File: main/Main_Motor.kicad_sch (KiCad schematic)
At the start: 3 parts

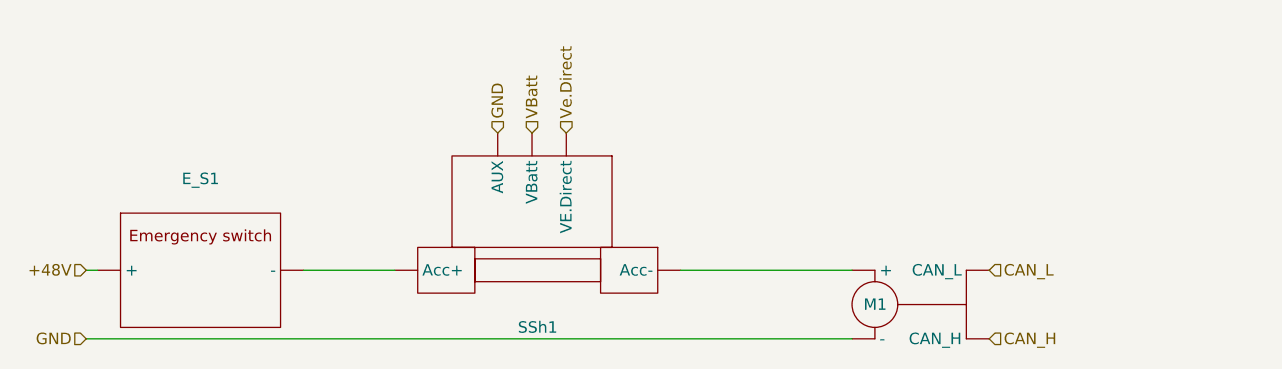
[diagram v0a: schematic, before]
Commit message: added UI, +12/gnd to 4 pin adapter symbol, added NMEA2000 gateway symbol
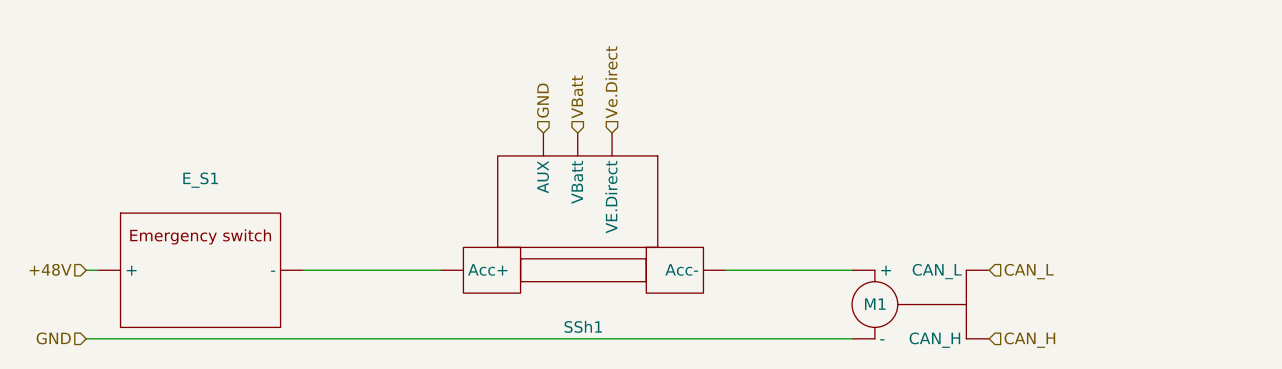
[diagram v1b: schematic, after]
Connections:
- new net: M1. (CAN_L), SSh1. (VE.Direct)
- new net: E_S1. (-), SSh1. (VE.Direct)
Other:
- moved on the sheet: SSh1
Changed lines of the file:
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@@
 	(wire
 		(pts
-			(xy 96.52 96.52) (xy 106.68 96.52)
+			(xy 143.51 96.52) (xy 157.48 96.52)
 		)
 		(stroke
@@
 	(wire
 		(pts
-			(xy 138.43 96.52) (xy 157.48 96.52)
+			(xy 111.76 96.52) (xy 96.52 96.52)
 		)
 		(stroke
@@
 	(hierarchical_label "GND"
 		(shape input)
-		(at 118.11 81.28 90)
+		(at 123.19 81.28 90)
 		(fields_autoplaced yes)
 		(effects
@@
 	(hierarchical_label "VBatt"
 		(shape input)
-		(at 121.92 81.28 90)
+		(at 127 81.28 90)
 		(fields_autoplaced yes)
 		(effects
@@
 	(hierarchical_label "Ve.Direct"
 		(shape input)
-		(at 125.73 81.28 90)
+		(at 130.81 81.28 90)
 		(fields_autoplaced yes)
 		(effects
@@
 	(symbol
 		(lib_id "New_Library_0:SmartShunt")
-		(at 121.92 88.9 270)
+		(at 127 88.9 270)
 		(unit 1)
 		(exclude_from_sim no)
@@
 		(fields_autoplaced yes)
 		(property "Reference" "SSh1"
-			(at 122.555 102.87 90)
+			(at 127.635 102.87 90)
 			(effects
 				(font
@@
 		)
 		(property "Value" "~"
-			(at 122.555 104.14 90)
+			(at 127.635 104.14 90)
 			(effects
 				(font
@@
 		)
 		(property "Footprint" ""
-			(at 122.555 95.885 90)
+			(at 127.635 95.885 90)
 			(effects
 				(font
@@
 		)
 		(property "Datasheet" ""
-			(at 122.555 95.885 90)
+			(at 127.635 95.885 90)
 			(effects
 				(font
@@
 		)
 		(property "Description" ""
-			(at 122.555 95.885 90)
+			(at 127.635 95.885 90)
 			(effects
 				(font

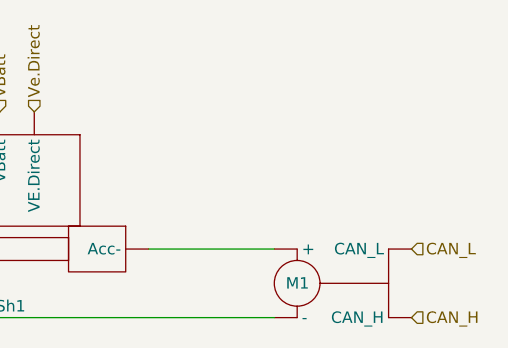
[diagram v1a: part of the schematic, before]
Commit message: added new output from main motor and connected it to NMEA input in monitor
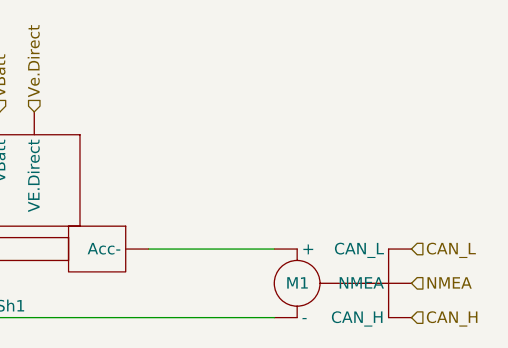
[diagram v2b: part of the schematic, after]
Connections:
- net NMEA: now reaches M1. (NMEA)
- net NMEA: no longer SSh1. (VE.Direct)
- new net: M1. (NMEA), SSh1. (VE.Direct)
- new net: E_S1. (-), SSh1. (VE.Direct)
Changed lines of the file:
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@@
+		)
+	)
+	(hierarchical_label "NMEA"
+		(shape input)
+		(at 172.72 100.33 0)
+		(fields_autoplaced yes)
+		(effects
+			(font
+				(size 1.27 1.27)
+			)
+			(justify left)
 		)
 	)
@@
 		)
 		(pin ""
+		)
+		(pin ""

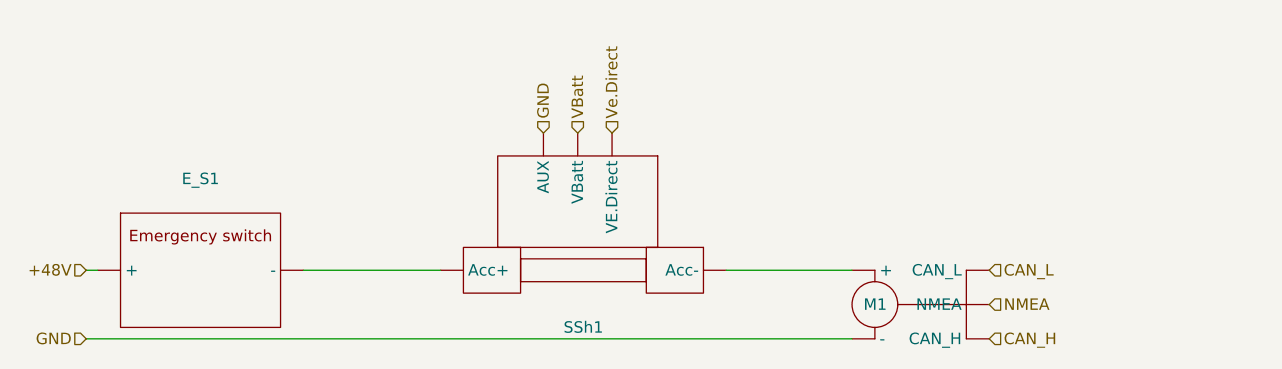
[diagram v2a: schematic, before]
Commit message: added emergency switch to mppt updateg seet layout
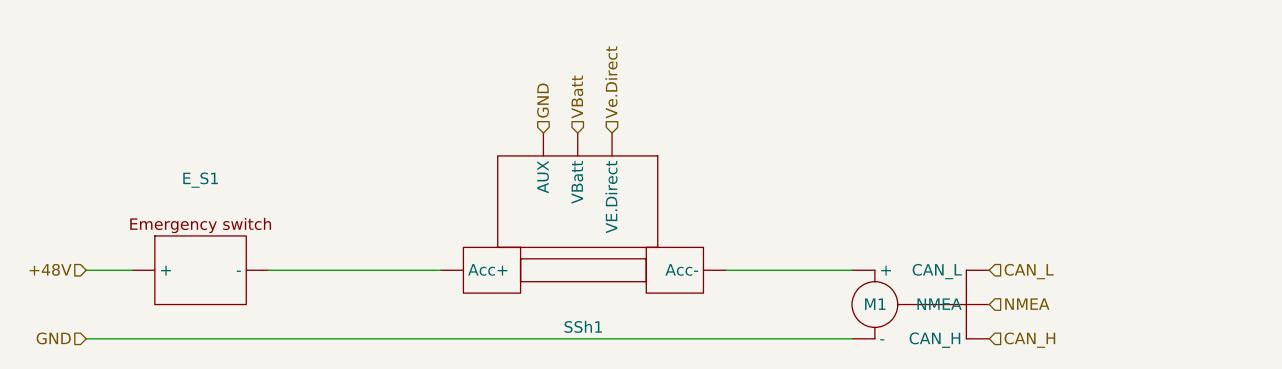
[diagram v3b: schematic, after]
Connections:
- new net: E_S1. (-), SSh1. (VE.Direct)
- new net: M1. (NMEA), SSh1. (VE.Direct)
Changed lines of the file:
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@@
 	(wire
 		(pts
-			(xy 73.66 96.52) (xy 72.39 96.52)
+			(xy 72.39 96.52) (xy 77.47 96.52)
 		)
 		(stroke
@@
 	(wire
 		(pts
-			(xy 72.39 104.14) (xy 157.48 104.14)
+			(xy 92.71 96.52) (xy 111.76 96.52)
 		)
 		(stroke
@@
 	(wire
 		(pts
-			(xy 143.51 96.52) (xy 157.48 96.52)
+			(xy 72.39 104.14) (xy 157.48 104.14)
 		)
 		(stroke
@@
 	(wire
 		(pts
-			(xy 111.76 96.52) (xy 96.52 96.52)
+			(xy 143.51 96.52) (xy 157.48 96.52)
 		)
 		(stroke
@@
 				(path "/54fbbba9-a737-4199-9a4b-f9fa49b3de5e/0e0ba13e-1f37-4579-8a2d-3eca3dc701e5"
 					(reference "SSh1")
+					(unit 1)
+				)
+			)
+		)
+	)
+	(symbol
+		(lib_id "New_Library_0:Emergency_Switch")
+		(at 85.09 96.52 0)
+		(unit 1)
+		(exclude_from_sim no)
+		(in_bom yes)
+		(on_board yes)
+		(dnp no)
+		(fields_autoplaced yes)
+		(property "Reference" "E_S1"
+			(at 85.09 86.36 0)
+			(effects
+				(font
+					(size 1.27 1.27)
+				)
+			)
+		)
+		(property "Value" "~"
+			(at 85.09 88.9 0)
+			(effects
+				(font
+					(size 1.27 1.27)
+				)
+			)
+		)
+		(property "Footprint" ""
+			(at 85.09 96.52 0)
+			(effects
+				(font
+					(size 1.27 1.27)
+				)
+				(hide yes)
+			)
+		)
+		(property "Datasheet" ""
+			(at 85.09 96.52 0)
+			(effects
+				(font
+					(size 1.27 1.27)
+				)
+				(hide yes)
+			)
+		)
+		(property "Description" ""
+			(at 85.09 96.52 0)
+			(effects
+				(font
+					(size 1.27 1.27)
+				)
+				(hide yes)
+			)
+		)
+		(pin ""
+		)
+		(pin ""
+		)
+		(instances
+			(project ""
+				(path "/54fbbba9-a737-4199-9a4b-f9fa49b3de5e/0e0ba13e-1f37-4579-8a2d-3eca3dc701e5"
+					(reference "E_S1")
 					(unit 1)
 				)
@@
 					(unit 1)
 				)
-			)
-		)
-	)
-	(symbol
-		(lib_id "New_Library_0:Emergency_Switch")
-		(at 85.09 96.52 0)
-		(unit 1)
-		(exclude_from_sim no)
-		(in_bom yes)
-		(on_board yes)
-		(dnp no)
-		(fields_autoplaced yes)
-		(property "Reference" "E_S1"
-			(at 85.09 86.36 0)
-			(effects
-				(font
-					(size 1.27 1.27)
-				)
-			)
-		)
-		(property "Value" "~"
-			(at 85.09 88.9 0)
-			(effects
-				(font
-					(size 1.27 1.27)
-				)
-			)
-		)
-		(property "Footprint" ""
-			(at 85.09 96.52 0)
-			(effects
-				(font
-					(size 1.27 1.27)
-				)
-				(hide yes)
-			)
-		)
-		(property "Datasheet" ""
-			(at 85.09 96.52 0)
-			(effects
-				(font
-					(size 1.27 1.27)
-				)
-				(hide yes)
-			)
-		)
-		(property "Description" ""
-			(at 85.09 96.52 0)
-			(effects
-				(font
-					(size 1.27 1.27)
-				)
-				(hide yes)
-			)
-		)
-		(pin ""
-		)
-		(pin ""
-		)
-		(instances
-			(project ""
-				(path "/54fbbba9-a737-4199-9a4b-f9fa49b3de5e/0e0ba13e-1f37-4579-8a2d-3eca3dc701e5"
-					(reference "E_S1")
-					(unit 1)
-				)

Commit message: added logos, oranised sheets, final version
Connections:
- new net: E_S1. (-), SSh1. (VE.Direct)
- new net: M1. (NMEA), SSh1. (VE.Direct)
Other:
- company: (none) -> Designers: Krzysztof Grajek, Wojtek Kołodziej
- title: (none) -> Main motor schematic

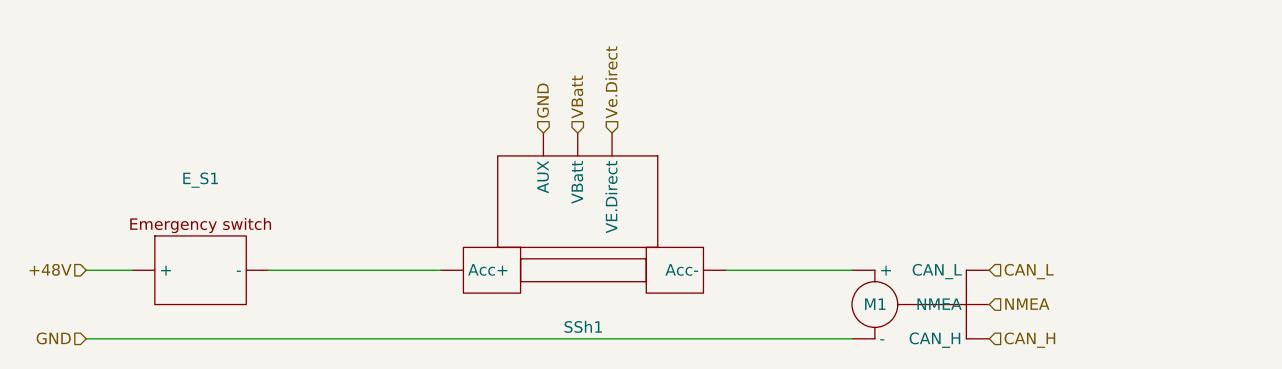
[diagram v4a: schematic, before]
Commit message: added nwe sheet (switching system), created a few new symbols, changed +48V coming from battery to Battery_High_voltage,
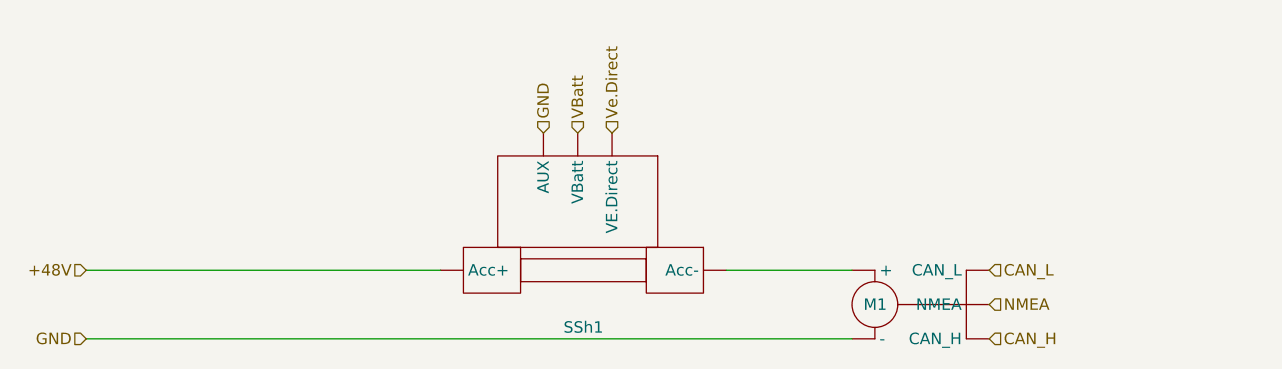
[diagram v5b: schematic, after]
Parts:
- removed E_S1: ~, symbol New_Library_0:Emergency_Switch
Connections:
- net +48V: now also SSh1. (VE.Direct)
- new net: M1. (NMEA), SSh1. (VE.Direct)
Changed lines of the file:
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@@
 	(wire
 		(pts
-			(xy 72.39 96.52) (xy 77.47 96.52)
-		)
-		(stroke
-			(width 0)
-			(type default)
-		)
-	)
-	(wire
-		(pts
-			(xy 92.71 96.52) (xy 111.76 96.52)
+			(xy 72.39 96.52) (xy 111.76 96.52)
 		)
 		(stroke
@@
 					(unit 1)
 				)
-			)
-		)
-	)
-	(symbol
-		(lib_id "New_Library_0:Emergency_Switch")
-		(at 85.09 96.52 0)
-		(unit 1)
-		(exclude_from_sim no)
-		(in_bom yes)
-		(on_board yes)
-		(dnp no)
-		(fields_autoplaced yes)
-		(property "Reference" "E_S1"
-			(at 85.09 86.36 0)
-			(effects
-				(font
-					(size 1.27 1.27)
-				)
-			)
-		)
-		(property "Value" "~"
-			(at 85.09 88.9 0)
-			(effects
-				(font
-					(size 1.27 1.27)
-				)
-			)
-		)
-		(property "Footprint" ""
-			(at 85.09 96.52 0)
-			(effects
-				(font
-					(size 1.27 1.27)
-				)
-				(hide yes)
-			)
-		)
-		(property "Datasheet" ""
-			(at 85.09 96.52 0)
-			(effects
-				(font
-					(size 1.27 1.27)
-				)
-				(hide yes)
-			)
-		)
-		(property "Description" ""
-			(at 85.09 96.52 0)
-			(effects
-				(font
-					(size 1.27 1.27)
-				)
-				(hide yes)
-			)
-		)
-		(pin ""
-		)
-		(pin ""
-		)
-		(instances
-			(project ""
-				(path "/54fbbba9-a737-4199-9a4b-f9fa49b3de5e/0e0ba13e-1f37-4579-8a2d-3eca3dc701e5"
-					(reference "E_S1")
-					(unit 1)
-				)

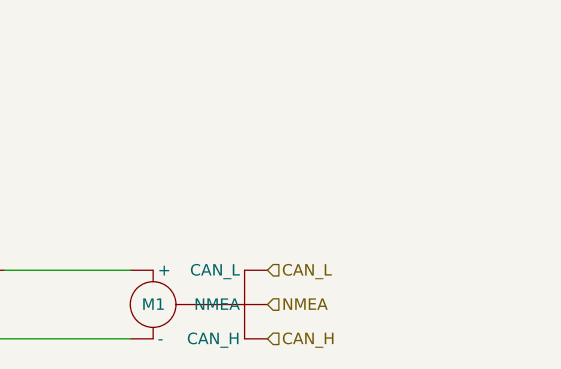
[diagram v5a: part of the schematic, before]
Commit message: added Digital Gateway in motor sheet
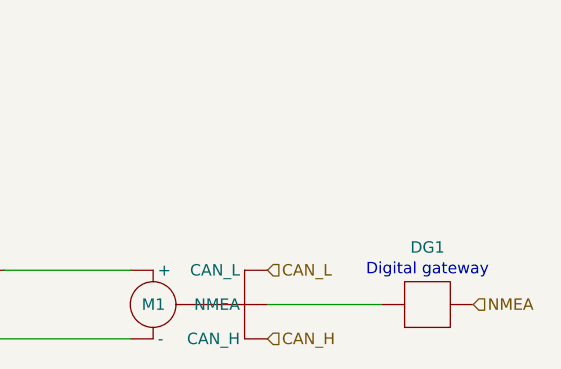
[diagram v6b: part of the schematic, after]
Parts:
- added DG1: ~, symbol New_Library_0:DigitalGateway
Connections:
- net NMEA: now also DG1.; no longer M1. (NMEA)
- new net: DG1., M1. (NMEA)
- new net: M1. (NMEA), SSh1. (VE.Direct)
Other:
- note added: "Digital gateway"
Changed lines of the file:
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@@
+		)
+	)
+	(wire
+		(pts
+			(xy 172.72 100.33) (xy 185.42 100.33)
+		)
+		(stroke
+			(width 0)
+			(type default)
 		)
 	)
@@
 		)
 	)
+	(text "Digital gateway"
+		(exclude_from_sim no)
+		(at 190.5 96.52 0)
+		(effects
+			(font
+				(size 1.27 1.27)
+			)
+		)
+	)
 	(hierarchical_label "CAN_H"
 		(shape input)
@@
 		)
 	)
-	(hierarchical_label "NMEA"
-		(shape input)
-		(at 172.72 100.33 0)
-		(fields_autoplaced yes)
-		(effects
-			(font
-				(size 1.27 1.27)
-			)
-			(justify left)
-		)
-	)
 	(hierarchical_label "GND"
 		(shape input)
@@
 		)
 	)
+	(hierarchical_label "NMEA"
+		(shape input)
+		(at 195.58 100.33 0)
+		(fields_autoplaced yes)
+		(effects
+			(font
+				(size 1.27 1.27)
+			)
+			(justify left)
+		)
+	)
+	(symbol
+		(lib_id "New_Library_0:DigitalGateway")
+		(at 190.5 100.33 0)
+		(unit 1)
+		(exclude_from_sim no)
+		(in_bom yes)
+		(on_board yes)
+		(dnp no)
+		(fields_autoplaced yes)
+		(property "Reference" "DG1"
+			(at 190.5 93.98 0)
+			(effects
+				(font
+					(size 1.27 1.27)
+				)
+			)
+		)
+		(property "Value" "~"
+			(at 190.5 96.52 0)
+			(effects
+				(font
+					(size 1.27 1.27)
+				)
+			)
+		)
+		(property "Footprint" ""
+			(at 190.5 100.33 0)
+			(effects
+				(font
+					(size 1.27 1.27)
+				)
+				(hide yes)
+			)
+		)
+		(property "Datasheet" ""
+			(at 190.5 100.33 0)
+			(effects
+				(font
+					(size 1.27 1.27)
+				)
+				(hide yes)
+			)
+		)
+		(property "Description" ""
+			(at 190.5 100.33 0)
+			(effects
+				(font
+					(size 1.27 1.27)
+				)
+				(hide yes)
+			)
+		)
+		(pin ""
+		)
+		(pin ""
+		)
+		(instances
+			(project ""
+				(path "/54fbbba9-a737-4199-9a4b-f9fa49b3de5e/0e0ba13e-1f37-4579-8a2d-3eca3dc701e5"
+					(reference "DG1")
+					(unit 1)
+				)
+			)
+		)
+	)

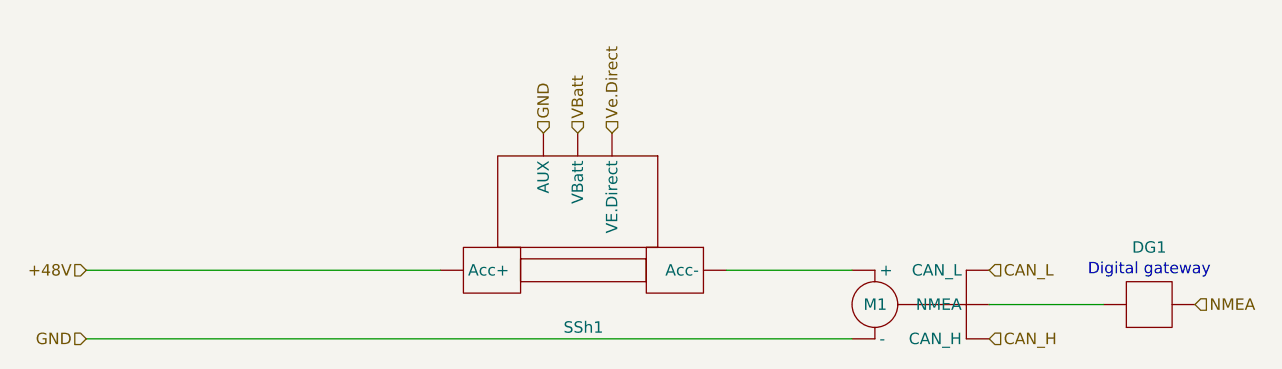
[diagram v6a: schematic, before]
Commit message: Updated digital gateway position. Removed NMEA lines
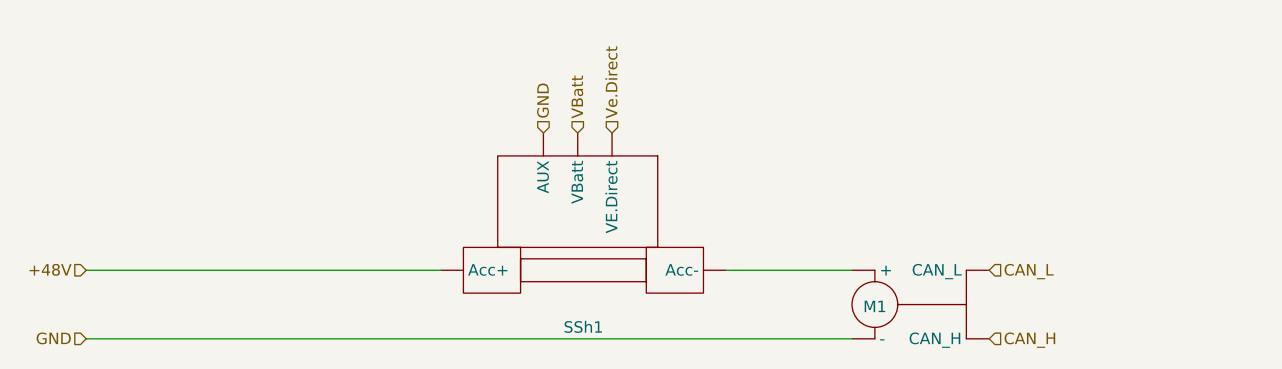
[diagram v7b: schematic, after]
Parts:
- removed DG1: ~, symbol New_Library_0:DigitalGateway
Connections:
- new net: M1. (CAN_L), SSh1. (VE.Direct)
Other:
- note removed: "Digital gateway"
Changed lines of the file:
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@@
-		)
-	)
-	(wire
-		(pts
-			(xy 172.72 100.33) (xy 185.42 100.33)
-		)
-		(stroke
-			(width 0)
-			(type default)
 		)
 	)
@@
 		)
 	)
-	(text "Digital gateway"
-		(exclude_from_sim no)
-		(at 190.5 96.52 0)
-		(effects
-			(font
-				(size 1.27 1.27)
-			)
-		)
-	)
 	(hierarchical_label "CAN_H"
 		(shape input)
@@
 		)
 	)
-	(hierarchical_label "NMEA"
-		(shape input)
-		(at 195.58 100.33 0)
-		(fields_autoplaced yes)
-		(effects
-			(font
-				(size 1.27 1.27)
-			)
-			(justify left)
-		)
-	)
 	(symbol
-		(lib_id "New_Library_0:DigitalGateway")
-		(at 190.5 100.33 0)
+		(lib_id "New_Library_0:Motor")
+		(at 160.02 100.33 0)
 		(unit 1)
 		(exclude_from_sim no)
@@
 		(on_board yes)
 		(dnp no)
-		(fields_autoplaced yes)
-		(property "Reference" "DG1"
-			(at 190.5 93.98 0)
+		(property "Reference" "M1"
+			(at 160.02 100.584 0)
 			(effects
 				(font
@@
 		)
 		(property "Value" "~"
-			(at 190.5 96.52 0)
+			(at 163.83 95.25 0)
 			(effects
 				(font
@@
 		)
 		(property "Footprint" ""
-			(at 190.5 100.33 0)
+			(at 160.02 100.33 0)
 			(effects
 				(font
@@
 		)
 		(property "Datasheet" ""
-			(at 190.5 100.33 0)
+			(at 160.02 100.33 0)
 			(effects
 				(font
@@
 		)
 		(property "Description" ""
-			(at 190.5 100.33 0)
+			(at 160.02 100.33 0)
 			(effects
 				(font
@@
 		(pin ""
 		)
+		(pin ""
+		)
+		(pin ""
+		)
 		(instances
 			(project ""
 				(path "/54fbbba9-a737-4199-9a4b-f9fa49b3de5e/0e0ba13e-1f37-4579-8a2d-3eca3dc701e5"
-					(reference "DG1")
+					(reference "M1")
 					(unit 1)
 				)
@@
 					(unit 1)
 				)
-			)
-		)
-	)
-	(symbol
-		(lib_id "New_Library_0:Motor")
-		(at 160.02 100.33 0)
-		(unit 1)
-		(exclude_from_sim no)
-		(in_bom yes)
-		(on_board yes)
-		(dnp no)
-		(property "Reference" "M1"
-			(at 158.75 100.33 0)
-			(effects
-				(font
-					(size 1.27 1.27)
-				)
-				(justify left)
-			)
-		)
-		(property "Value" "~"
-			(at 163.83 101.6 0)
-			(effects
-				(font
-					(size 1.27 1.27)
-				)
-				(justify left)
-			)
-		)
-		(property "Footprint" ""
-			(at 160.02 100.33 0)
-			(effects
-				(font
-					(size 1.27 1.27)
-				)
-				(hide yes)
-			)
-		)
-		(property "Datasheet" ""
-			(at 160.02 100.33 0)
-			(effects
-				(font
-					(size 1.27 1.27)
-				)
-				(hide yes)
-			)
-		)
-		(property "Description" ""
-			(at 160.02 100.33 0)
-			(effects
-				(font
-					(size 1.27 1.27)
-				)
-				(hide yes)
-			)
-		)
-		(pin ""
-		)
-		(pin ""
-		)
-		(pin ""
-		)
-		(pin ""
-		)
-		(pin ""
-		)
-		(instances
-			(project ""
-				(path "/54fbbba9-a737-4199-9a4b-f9fa49b3de5e/0e0ba13e-1f37-4579-8a2d-3eca3dc701e5"
-					(reference "M1")
-					(unit 1)
-				)
